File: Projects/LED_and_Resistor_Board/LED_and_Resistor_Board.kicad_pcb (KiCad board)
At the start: 2 copper layers, 54.6 x 12.7 mm, 4 parts

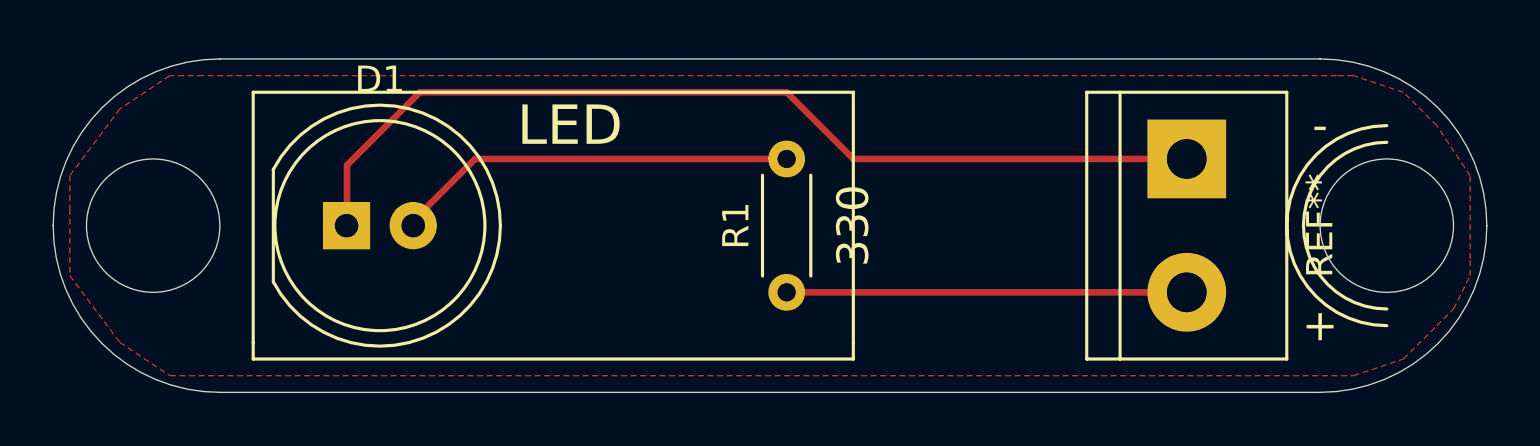
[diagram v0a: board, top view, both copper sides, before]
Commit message: Add header to Schematic and change PCB - no more DRC errors
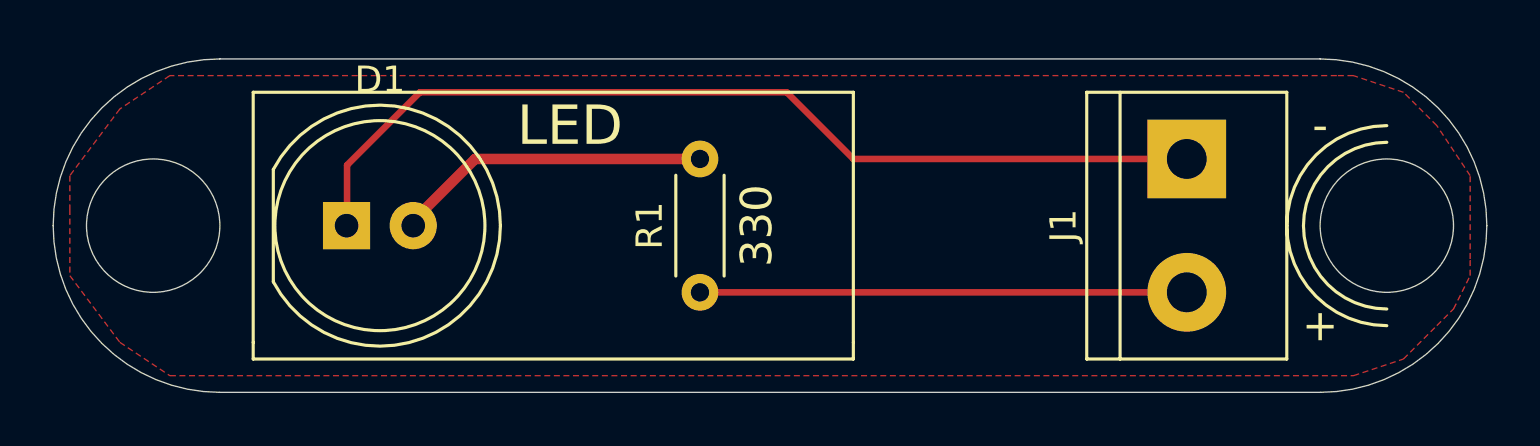
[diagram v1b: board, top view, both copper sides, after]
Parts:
- removed the REF** at (172.7, 96.5)
- added J1: Conn_01x02_Male, TerminalBlock:TerminalBlock_bornier-2_P5.08mm, F.Cu at (172.7, 96.5)
- moved R1 3.30 mm to (154.2, 101.6)
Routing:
- net GND: track 0.00 -> 36.3 mm
- net (no net): track 36.3 -> 0.00 mm
- net Net-(D1-Pad2): track 15.2 -> 11.9 mm
- net +5V: track 15.9 -> 18.5 mm
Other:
- net class PWR added: clearance 0.2, trace_width 0.4, via_dia 0.8, via_drill 0.4
